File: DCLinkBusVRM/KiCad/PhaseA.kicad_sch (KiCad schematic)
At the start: 34 parts, among them IC8 LM358DR, Q1 IMBG65R015M2H, Q4 IMBG65R015M2H, U6 ACS758xCB-200U-PFF

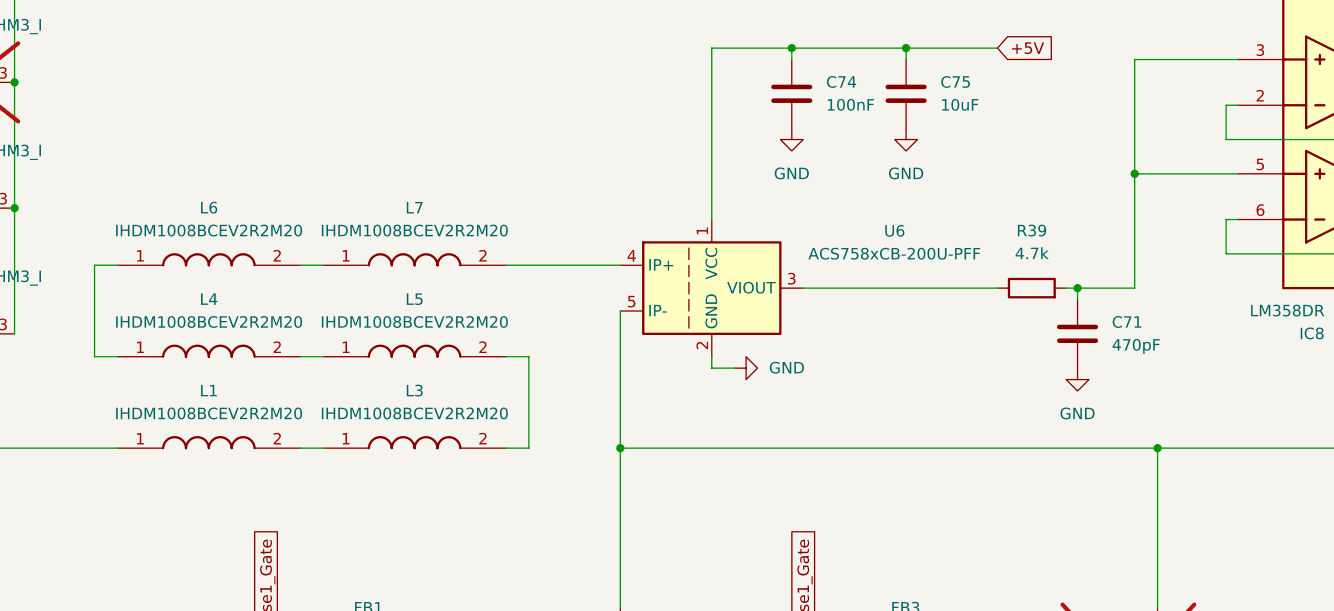
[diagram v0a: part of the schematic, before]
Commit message: Update boost converter, add dynamic brake grid, etc
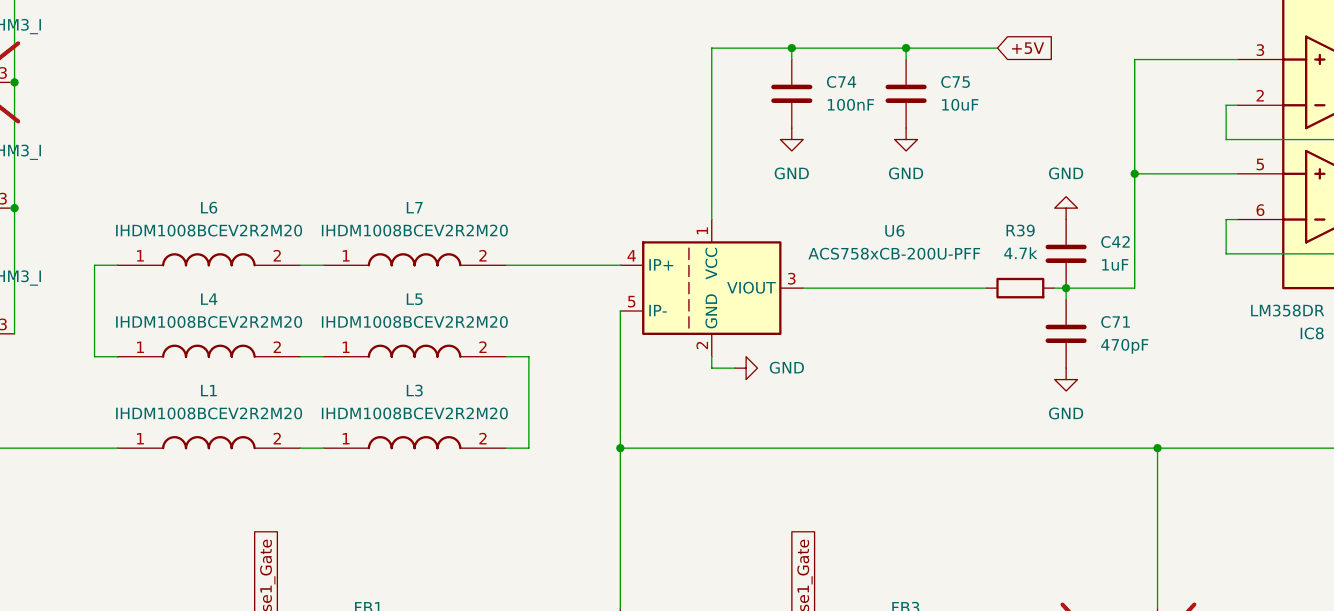
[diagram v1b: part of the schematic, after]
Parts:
- added C42: 1uF, Capacitor_SMD:C_1210_3225Metric_Pad1.33x2.70mm_HandSolder, symbol Device:C
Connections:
- net GND: now also C42.1
- net at C71.1, IC8.3 (IN1+), IC8.5 (IN2+)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: now also C42.2
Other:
- moved on the sheet: C71, R39
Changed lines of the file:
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@@
 (kicad_sch
-	(version 20231120)
+	(version 20250114)
 	(generator "eeschema")
-	(generator_version "8.0")
+	(generator_version "9.0")
 	(paper "A4")
 	(title_block
@@
 	)
 	(junction
+		(at 175.26 71.12)
+		(diameter 0)
+		(color 0 0 0 0)
+	)
+	(junction
 		(at 48.26 59.69)
 		(diameter 0)
@@
 		(color 0 0 0 0)
 	)
-	(junction
-		(at 176.53 71.12)
-		(diameter 0)
-		(color 0 0 0 0)
-	)
 	(wire
 		(pts
@@
 	(wire
 		(pts
-			(xy 175.26 71.12) (xy 176.53 71.12)
+			(xy 173.99 71.12) (xy 175.26 71.12)
 		)
 		(stroke
@@
 	(wire
 		(pts
-			(xy 146.05 71.12) (xy 167.64 71.12)
+			(xy 146.05 71.12) (xy 166.37 71.12)
 		)
 		(stroke
@@
 	(wire
 		(pts
-			(xy 176.53 71.12) (xy 182.88 71.12)
-		)
-		(stroke
-			(width 0)
-			(type default)
-		)
-	)
-	(wire
-		(pts
 			(xy 113.03 88.9) (xy 115.57 88.9)
 		)
@@
 	(wire
 		(pts
-			(xy 176.53 71.12) (xy 176.53 72.39)
+			(xy 175.26 71.12) (xy 175.26 72.39)
 		)
 		(stroke
@@
 	(wire
 		(pts
+			(xy 175.26 71.12) (xy 182.88 71.12)
+		)
+		(stroke
+			(width 0)
+			(type default)
+		)
+	)
+	(wire
+		(pts
 			(xy 222.25 25.4) (xy 222.25 24.13)
 		)
@@
 	(symbol
 		(lib_id "power:GND")
-		(at 176.53 80.01 0)
+		(at 175.26 80.01 0)
 		(unit 1)
 		(exclude_from_sim no)
@@
 		(fields_autoplaced yes)
 		(property "Reference" "#PWR0100"
-			(at 176.53 86.36 0)
+			(at 175.26 86.36 0)
 			(effects
 				(font
@@
 		)
 		(property "Value" "GND"
-			(at 176.53 85.09 0)
+			(at 175.26 85.09 0)
 			(effects
 				(font
@@
 		)
 		(property "Footprint" ""
-			(at 176.53 80.01 0)
+			(at 175.26 80.01 0)
 			(effects
 				(font
@@
 		)
 		(property "Datasheet" ""
-			(at 176.53 80.01 0)
+			(at 175.26 80.01 0)
 			(effects
 				(font
@@
 		)
 		(property "Description" "Power symbol creates a global label with name \"GND\" , ground"
-			(at 176.53 80.01 0)
+			(at 175.26 80.01 0)
 			(effects
 				(font
@@
 	(symbol
 		(lib_id "Device:C")
+		(at 175.26 67.31 0)
+		(unit 1)
+		(exclude_from_sim no)
+		(in_bom yes)
+		(on_board yes)
+		(dnp no)
+		(fields_autoplaced yes)
+		(property "Reference" "C42"
+			(at 179.07 66.0399 0)
+			(effects
+				(font
+					(size 1.27 1.27)
+				)
+				(justify left)
+			)
+		)
+		(property "Value" "1uF"
+			(at 179.07 68.5799 0)
+			(effects
+				(font
+					(size 1.27 1.27)
+				)
+				(justify left)
+			)
+		)
+		(property "Footprint" "Capacitor_SMD:C_1210_3225Metric_Pad1.33x2.70mm_HandSolder"
+			(at 176.2252 71.12 0)
+			(effects
+				(font
+					(size 1.27 1.27)
+				)
+				(hide yes)
+			)
+		)
+		(property "Datasheet" "~"
+			(at 175.26 67.31 0)
+			(effects
+				(font
+					(size 1.27 1.27)
+				)
+				(hide yes)
+			)
+		)
+		(property "Description" "Unpolarized capacitor"
+			(at 175.26 67.31 0)
+			(effects
+				(font
+					(size 1.27 1.27)
+				)
+				(hide yes)
+			)
+		)
+		(pin "1"
+		)
+		(pin "2"
+		)
+		(instances
+			(project "InverterBoostConverter_v2"
+				(path "/2b0bf6ef-6fb8-4b0f-8d72-c07d92ef1505/d364237d-c309-45a0-8ad7-401a789ba93d"
+					(reference "C42")
+					(unit 1)
+				)
+			)
+		)
+	)
+	(symbol
+		(lib_id "Device:C")
 		(at 234.95 29.21 0)
 		(unit 1)
@@
 	(symbol
 		(lib_id "power:GND")
+		(at 175.26 63.5 180)
+		(unit 1)
+		(exclude_from_sim no)
+		(in_bom yes)
+		(on_board yes)
+		(dnp no)
+		(fields_autoplaced yes)
+		(property "Reference" "#PWR0109"
+			(at 175.26 57.15 0)
+			(effects
+				(font
+					(size 1.27 1.27)
+				)
+				(hide yes)
+			)
+		)
+		(property "Value" "GND"
+			(at 175.26 58.42 0)
+			(effects
+				(font
+					(size 1.27 1.27)
+				)
+			)
+		)
+		(property "Footprint" ""
+			(at 175.26 63.5 0)
+			(effects
+				(font
+					(size 1.27 1.27)
+				)
+				(hide yes)
+			)
+		)
+		(property "Datasheet" ""
+			(at 175.26 63.5 0)
+			(effects
+				(font
+					(size 1.27 1.27)
+				)
+				(hide yes)
+			)
+		)
+		(property "Description" "Power symbol creates a global label with name \"GND\" , ground"
+			(at 175.26 63.5 0)
+			(effects
+				(font
+					(size 1.27 1.27)
+				)
+				(hide yes)
+			)
+		)
+		(pin "1"
+		)
+		(instances
+			(project "InverterBoostConverter_v2"
+				(path "/2b0bf6ef-6fb8-4b0f-8d72-c07d92ef1505/d364237d-c309-45a0-8ad7-401a789ba93d"
+					(reference "#PWR0109")
+					(unit 1)
+				)
+			)
+		)
+	)
+	(symbol
+		(lib_id "power:GND")
 		(at 144.78 53.34 0)
 		(unit 1)
@@
 	(symbol
 		(lib_id "Device:R")
-		(at 171.45 71.12 90)
+		(at 170.18 71.12 90)
 		(unit 1)
 		(exclude_from_sim no)
@@
 		(fields_autoplaced yes)
 		(property "Reference" "R39"
-			(at 171.45 64.77 90)
+			(at 170.18 64.77 90)
 			(effects
 				(font
@@
 		)
 		(property "Value" "4.7k"
-			(at 171.45 67.31 90)
+			(at 170.18 67.31 90)
 			(effects
 				(font
@@
 		)
 		(property "Footprint" "Resistor_SMD:R_1210_3225Metric_Pad1.30x2.65mm_HandSolder"
-			(at 171.45 72.898 90)
+			(at 170.18 72.898 90)
 			(effects
 				(font
@@
 		)
 		(property "Datasheet" "~"
-			(at 171.45 71.12 0)
+			(at 170.18 71.12 0)
 			(effects
 				(font
@@
 		)
 		(property "Description" "Resistor"
-			(at 171.45 71.12 0)
+			(at 170.18 71.12 0)
 			(effects
 				(font
@@
 	(symbol
 		(lib_id "Device:C")
-		(at 176.53 76.2 0)
+		(at 175.26 76.2 0)
 		(unit 1)
 		(exclude_from_sim no)
@@
 		(fields_autoplaced yes)
 		(property "Reference" "C71"
-			(at 180.34 74.9299 0)
+			(at 179.07 74.9299 0)
 			(effects
 				(font
@@
 		)
 		(property "Value" "470pF"
-			(at 180.34 77.4699 0)
+			(at 179.07 77.4699 0)
 			(effects
 				(font
@@
 		)
 		(property "Footprint" "Capacitor_SMD:C_1210_3225Metric_Pad1.33x2.70mm_HandSolder"
-			(at 177.4952 80.01 0)
+			(at 176.2252 80.01 0)
 			(effects
 				(font
@@
 		)
 		(property "Datasheet" "~"
-			(at 176.53 76.2 0)
+			(at 175.26 76.2 0)
 			(effects
 				(font
@@
 		)
 		(property "Description" "Unpolarized capacitor"
-			(at 176.53 76.2 0)
+			(at 175.26 76.2 0)
 			(effects
 				(font

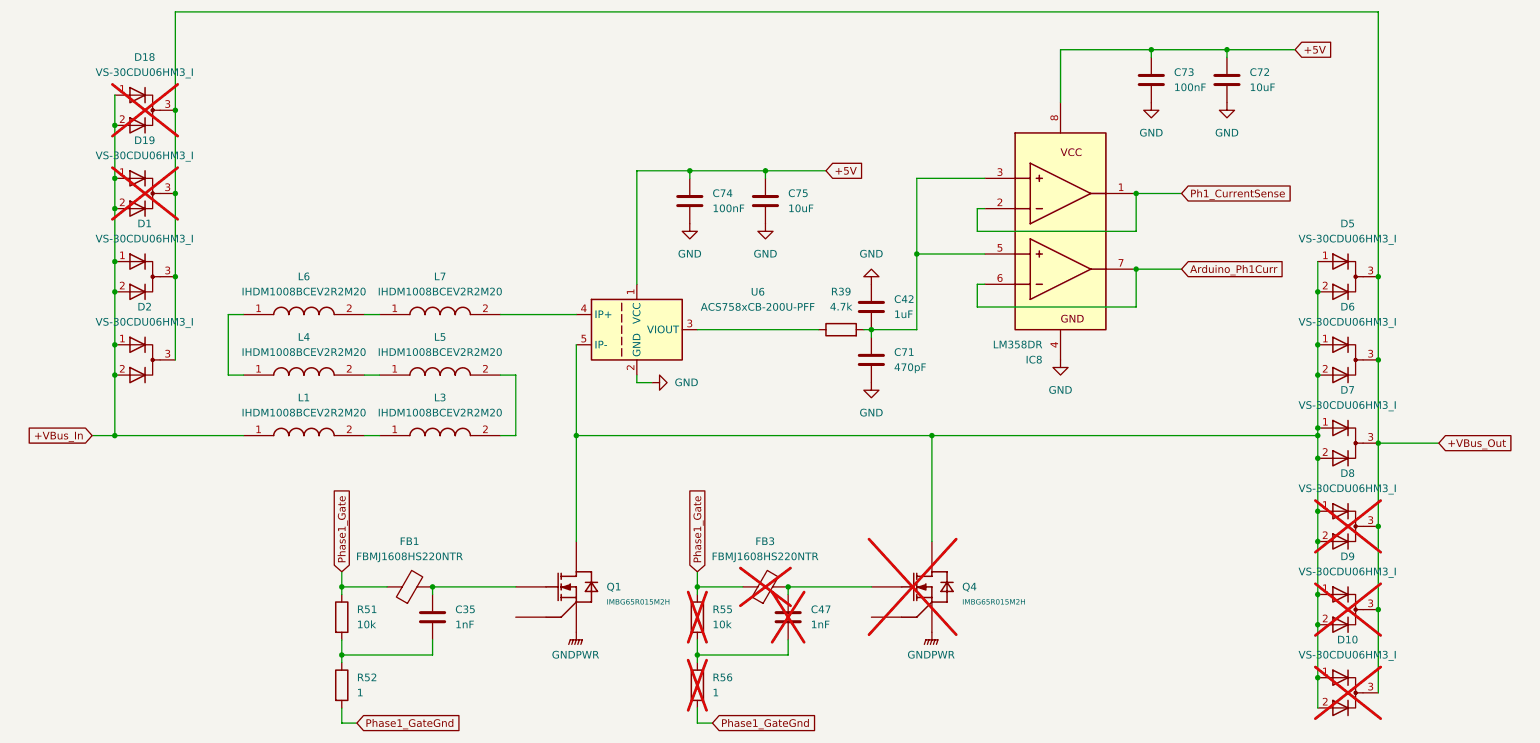
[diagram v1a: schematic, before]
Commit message: Update Canbus protocol for vrm
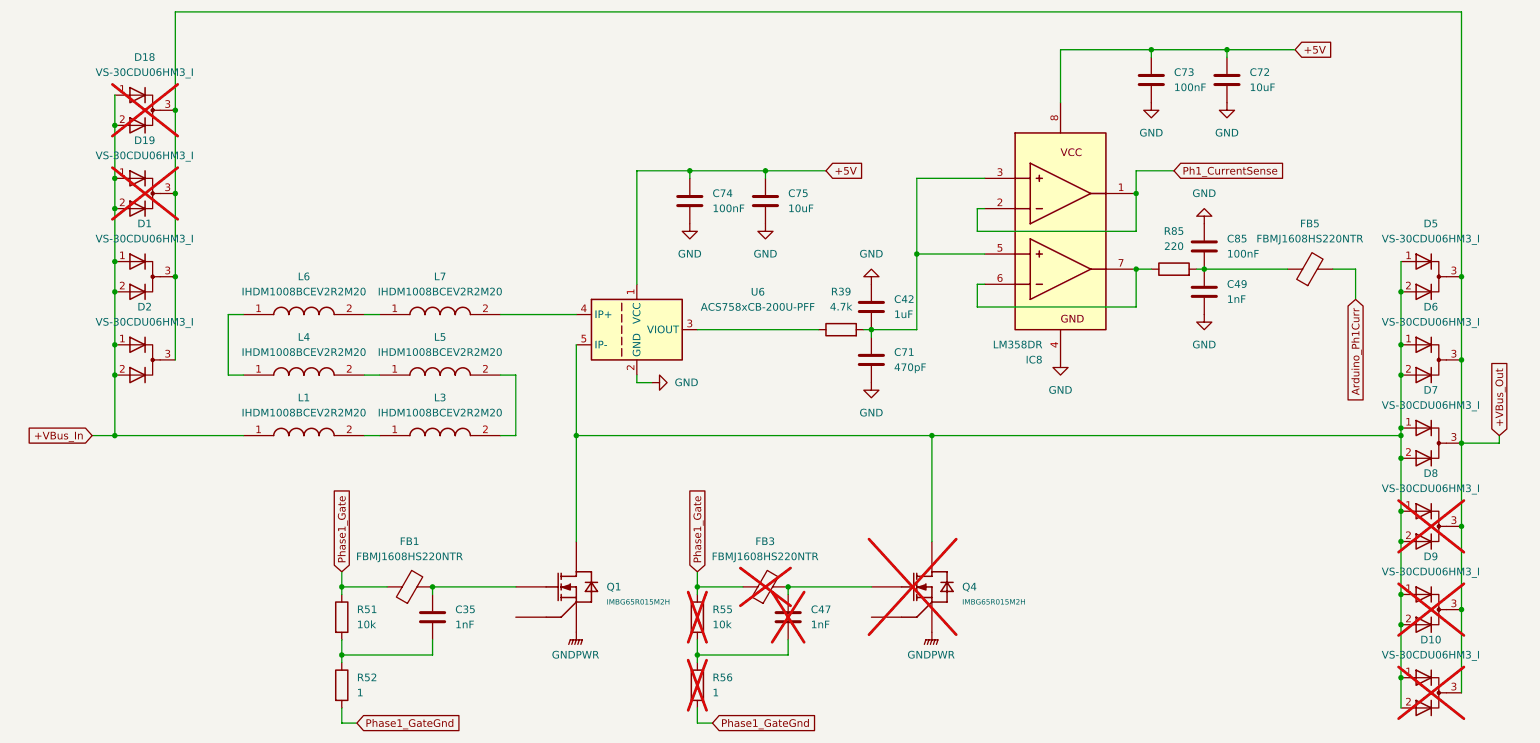
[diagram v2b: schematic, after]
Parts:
- added C49: 1nF, Capacitor_SMD:C_1210_3225Metric_Pad1.33x2.70mm_HandSolder, symbol Device:C
- added C85: 100nF, Capacitor_SMD:C_1210_3225Metric_Pad1.33x2.70mm_HandSolder, symbol Device:C
- added FB5: FBMJ1608HS220NTR, InverterCom:BEADC1608X100N, symbol Device:FerriteBead
- added R85: 220, Resistor_SMD:R_1210_3225Metric_Pad1.30x2.65mm_HandSolder, symbol Device:R
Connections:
- net Arduino_Ph1Curr: now also FB5.2; no longer IC8.6 (IN2-), IC8.7 (OUT2)
- net GND: now also C49.1, C85.1
- new net: C49.2, C85.2, FB5.1, R85.2
- new net: IC8.6 (IN2-), IC8.7 (OUT2), R85.1
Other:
- moved on the sheet: D10, D5, D6, D7, D8, D9
